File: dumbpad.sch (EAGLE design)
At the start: 40 parts

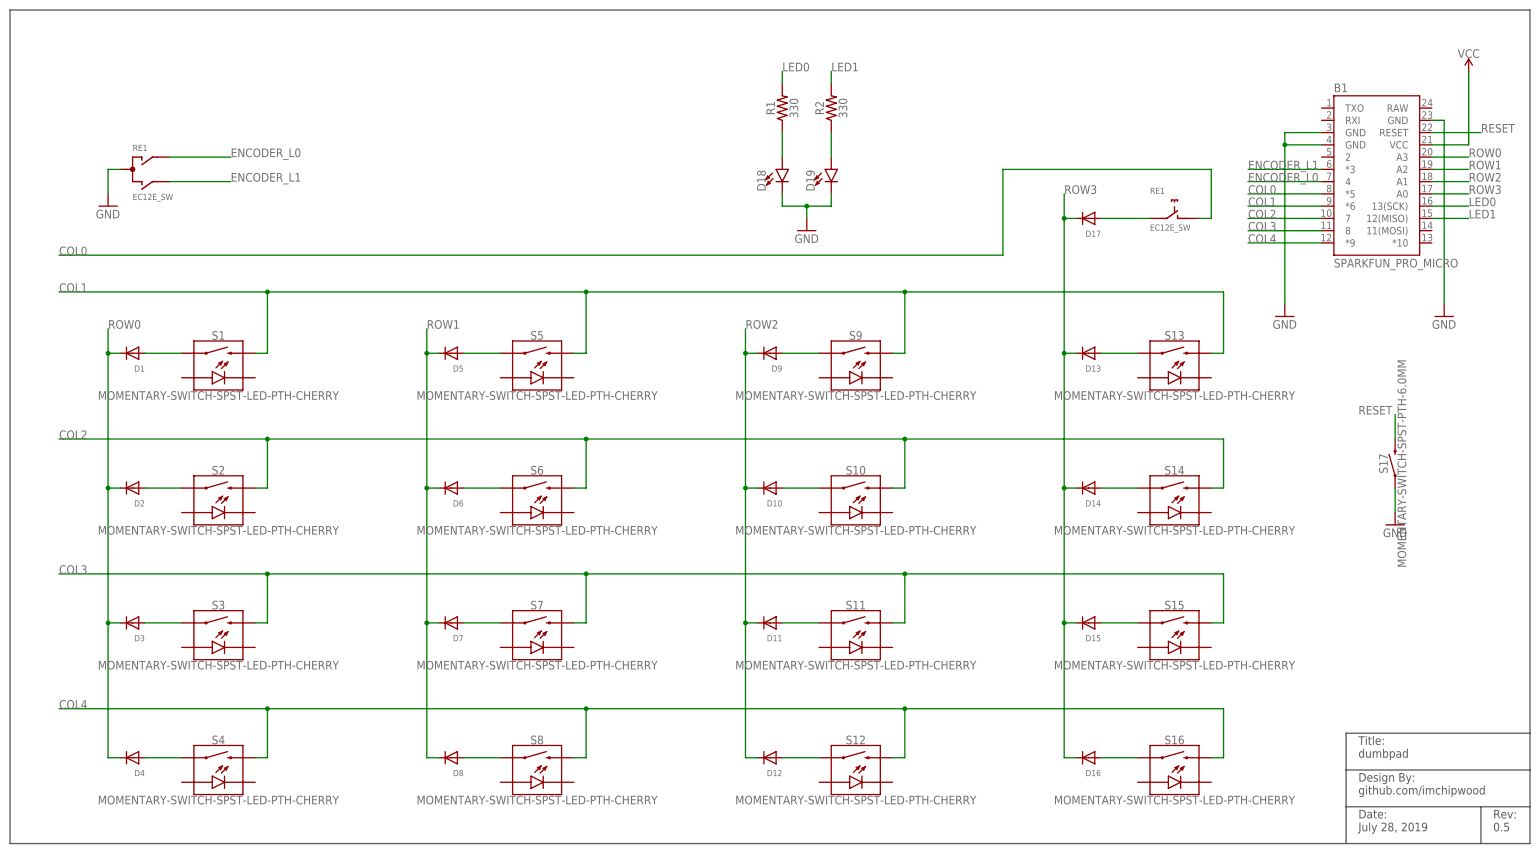
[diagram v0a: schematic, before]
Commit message: using reversible sockets
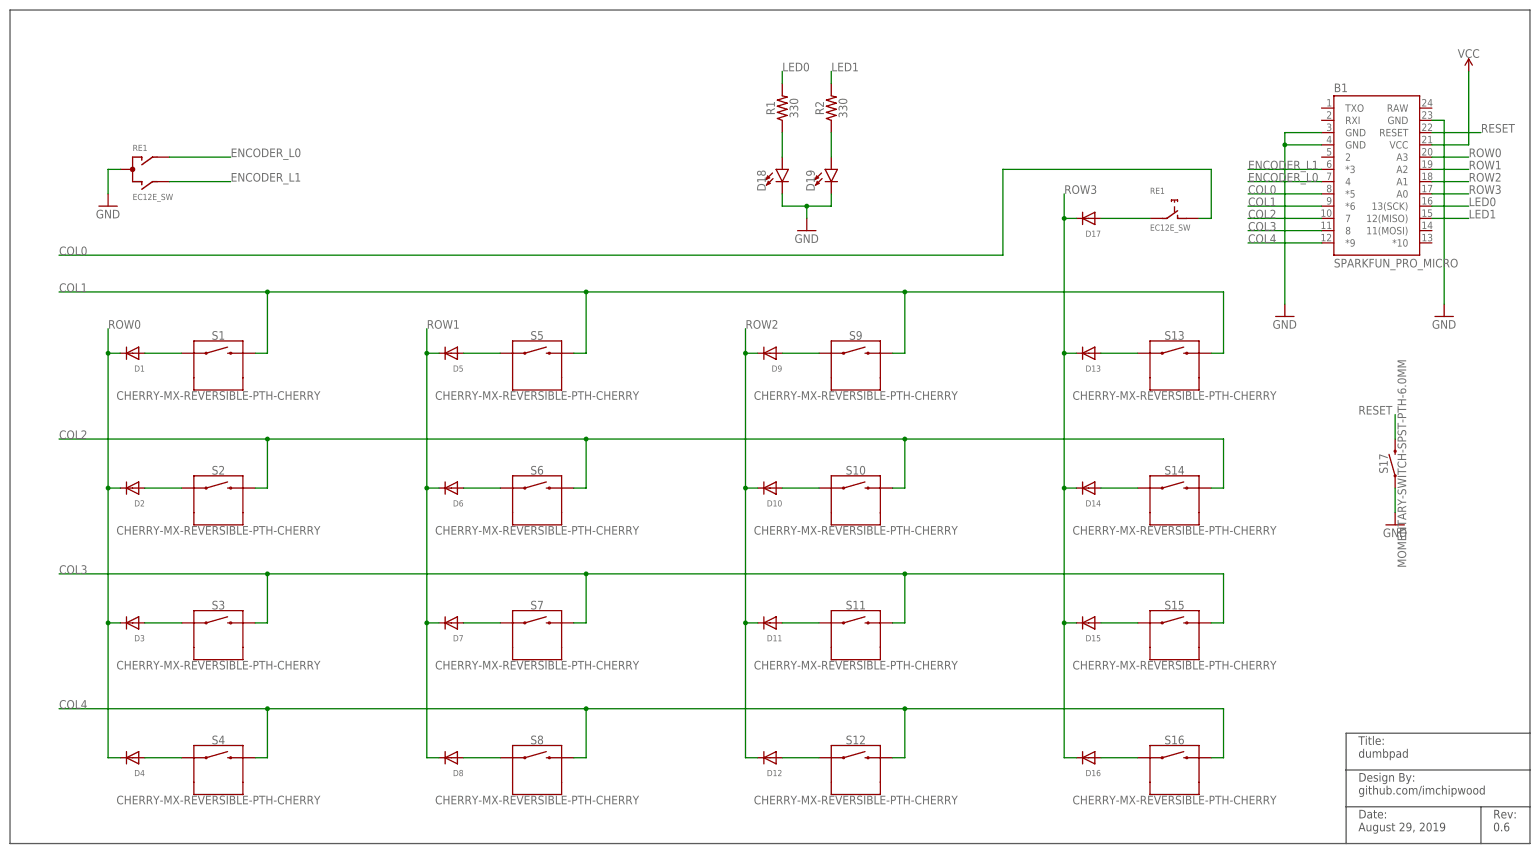
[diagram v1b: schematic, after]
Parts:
- S1, S10, S11, S12, S13, S14, S15, S16, S2, S3, S4, S5, S6, S7, S8, S9: value MOMENTARY-SWITCH-SPST-LED-PTH-CHERRY -> CHERRY-MX-REVERSIBLE-PTH-CHERRY; device SparkFun-Switches:MOMENTARY-SWITCH-SPST-LED-PTH-CHERRY -> cpwood:CHERRY-MX-REVERSIBLE-PTH-CHERRY
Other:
- note added: "Date: August 29, 2019"
- note added: "Rev: 0.6"
- note removed: "Date: July 28, 2019"
- note removed: "Rev: 0.5"
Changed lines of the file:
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@@
 </classes>
 <parts>
-<part name="S1" library="SparkFun-Switches" deviceset="MOMENTARY-SWITCH-SPST-LED" device="-PTH-CHERRY"/>
+<part name="S1" library="cpwood" deviceset="CHERRY-MX-REVERSIBLE" device="-PTH-CHERRY"/>
 <part name="B1" library="SparkFun-Boards" deviceset="SPARKFUN_PRO_MICRO" device=""/>
 <part name="RE1" library="switch-alps" library_urn="urn:adsk.eagle:library:373" deviceset="EC12E_SW" device="" package3d_urn="urn:adsk.eagle:package:27083/1"/>
 <part name="GND1" library="supply1" library_urn="urn:adsk.eagle:library:371" deviceset="GND" device=""/>
-<part name="S2" library="SparkFun-Switches" deviceset="MOMENTARY-SWITCH-SPST-LED" device="-PTH-CHERRY"/>
-<part name="S3" library="SparkFun-Switches" deviceset="MOMENTARY-SWITCH-SPST-LED" device="-PTH-CHERRY"/>
-<part name="S4" library="SparkFun-Switches" deviceset="MOMENTARY-SWITCH-SPST-LED" device="-PTH-CHERRY"/>
-<part name="S5" library="SparkFun-Switches" deviceset="MOMENTARY-SWITCH-SPST-LED" device="-PTH-CHERRY"/>
-<part name="S6" library="SparkFun-Switches" deviceset="MOMENTARY-SWITCH-SPST-LED" device="-PTH-CHERRY"/>
-<part name="S7" library="SparkFun-Switches" deviceset="MOMENTARY-SWITCH-SPST-LED" device="-PTH-CHERRY"/>
-<part name="S8" library="SparkFun-Switches" deviceset="MOMENTARY-SWITCH-SPST-LED" device="-PTH-CHERRY"/>
+<part name="S2" library="cpwood" deviceset="CHERRY-MX-REVERSIBLE" device="-PTH-CHERRY"/>
+<part name="S3" library="cpwood" deviceset="CHERRY-MX-REVERSIBLE" device="-PTH-CHERRY"/>
+<part name="S4" library="cpwood" deviceset="CHERRY-MX-REVERSIBLE" device="-PTH-CHERRY"/>
+<part name="S5" library="cpwood" deviceset="CHERRY-MX-REVERSIBLE" device="-PTH-CHERRY"/>
+<part name="S6" library="cpwood" deviceset="CHERRY-MX-REVERSIBLE" device="-PTH-CHERRY"/>
+<part name="S7" library="cpwood" deviceset="CHERRY-MX-REVERSIBLE" device="-PTH-CHERRY"/>
+<part name="S8" library="cpwood" deviceset="CHERRY-MX-REVERSIBLE" device="-PTH-CHERRY"/>
 <part name="GND7" library="supply1" library_urn="urn:adsk.eagle:library:371" deviceset="GND" device=""/>
-<part name="S9" library="SparkFun-Switches" deviceset="MOMENTARY-SWITCH-SPST-LED" device="-PTH-CHERRY"/>
-<part name="S10" library="SparkFun-Switches" deviceset="MOMENTARY-SWITCH-SPST-LED" device="-PTH-CHERRY"/>
-<part name="S11" library="SparkFun-Switches" deviceset="MOMENTARY-SWITCH-SPST-LED" device="-PTH-CHERRY"/>
-<part name="S12" library="SparkFun-Switches" deviceset="MOMENTARY-SWITCH-SPST-LED" device="-PTH-CHERRY"/>
-<part name="S13" library="SparkFun-Switches" deviceset="MOMENTARY-SWITCH-SPST-LED" device="-PTH-CHERRY"/>
-<part name="S14" library="SparkFun-Switches" deviceset="MOMENTARY-SWITCH-SPST-LED" device="-PTH-CHERRY"/>
-<part name="S15" library="SparkFun-Switches" deviceset="MOMENTARY-SWITCH-SPST-LED" device="-PTH-CHERRY"/>
-<part name="S16" library="SparkFun-Switches" deviceset="MOMENTARY-SWITCH-SPST-LED" device="-PTH-CHERRY"/>
+<part name="S9" library="cpwood" deviceset="CHERRY-MX-REVERSIBLE" device="-PTH-CHERRY"/>
+<part name="S10" library="cpwood" deviceset="CHERRY-MX-REVERSIBLE" device="-PTH-CHERRY"/>
+<part name="S11" library="cpwood" deviceset="CHERRY-MX-REVERSIBLE" device="-PTH-CHERRY"/>
+<part name="S12" library="cpwood" deviceset="CHERRY-MX-REVERSIBLE" device="-PTH-CHERRY"/>
+<part name="S13" library="cpwood" deviceset="CHERRY-MX-REVERSIBLE" device="-PTH-CHERRY"/>
+<part name="S14" library="cpwood" deviceset="CHERRY-MX-REVERSIBLE" device="-PTH-CHERRY"/>
+<part name="S15" library="cpwood" deviceset="CHERRY-MX-REVERSIBLE" device="-PTH-CHERRY"/>
+<part name="S16" library="cpwood" deviceset="CHERRY-MX-REVERSIBLE" device="-PTH-CHERRY"/>
 <part name="GND3" library="supply1" library_urn="urn:adsk.eagle:library:371" deviceset="GND" device=""/>
 <part name="SUPPLY2" library="SparkFun-PowerSymbols" deviceset="VCC" device=""/>
@@
 <wire x1="0" y1="172.72" x2="0" y2="0" width="0.1524" layer="97"/>
 <text x="307.34" y="2.54" size="1.778" layer="97">Rev:
-0.5</text>
+0.6</text>
 <text x="279.4" y="2.54" size="1.778" layer="97">Date:
-July 28, 2019</text>
+August 29, 2019</text>
 <text x="279.4" y="10.16" size="1.778" layer="97">Design By:
 github.com/imchipwood</text>
